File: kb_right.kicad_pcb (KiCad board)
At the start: 2 copper layers, 208.8 x 117.5 mm, 175 parts, among them J1 10029449-001RLF, J2 Conn_01x03, J3 Conn_01x06, J4 Conn_01x08, J5 Conn_01x09, SW0 RotaryEncoder_Switch

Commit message: added 1.75u right shift
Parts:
- added D32_1: D_Small, Diode_SMD:D_SOD-123, B.Cu at (197.9, 110.9)
- added MX32_1: MX-NoLED, MX_Only:MXOnly-1.75U-Hotswap, F.Cu at (162.7, 114.3)
- added MX32_2: MX-NoLED, MX_Only:MXOnly-1U-Hotswap, F.Cu at (188.9, 114.3)
- C101, C102, C103, C104, C105, C106, C107, C108, C109, C110, C111, C112, C113, C114, C115, C116, C117, C118, C119, C120, C121, C122, C123, C124, C125, C126, C127, C128, C129, C130, C131, C132, C133, C134, C135, C136, C137, C138, C139, C140, C141, C142: value C_Small -> 0.1uF
- MX32: footprint MX_Only:MXOnly-2.75U-Hotswap -> MX_Only:MXOnly-2.75U-Hotswap-ReversedStabilizers
- moved D32 27.5 mm to (155.6, 119.9)
- moved D133 17.9 mm to (172.2, 108.7), turned to 90 degrees
- moved C125 7.86 mm to (171.3, 102.5)
- moved D141 7.17 mm to (212.7, 143.7)
- moved D40 7.17 mm to (200.8, 143.7)
- moved D42 7.17 mm to (238.9, 143.7)
- moved D140 7.17 mm to (193.7, 143.7)
- moved D142 7.17 mm to (231.8, 143.7)
- moved D41 7.17 mm to (219.9, 143.7)
- moved D114 7.17 mm to (141.3, 81.8)
- moved D117 7.17 mm to (212.7, 81.8)
- moved D13 7.17 mm to (129.4, 81.8)
- moved D15 7.17 mm to (167.5, 81.8)
- moved D16 7.17 mm to (191.3, 81.8)
- moved D26 7.17 mm to (238.9, 81.8)
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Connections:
- J5 pad 1: /COL6 -> GND
- J5 pad 2: /ROW5 -> /COL6
- J5 pad 3: /ROW6 -> /ROW5
- J5 pad 4: /ROW7 -> /ROW6
- J5 pad 5: /ROW8 -> /ROW7
- J5 pad 6: /ROW9 -> /ROW8
- J5 pad 7: /COL7 -> /ROW9
- J5 pad 8: /COL8 -> /COL7
- J5 pad 9: GND -> /COL8
- MX32 pad 1: /COL6 -> /COL5
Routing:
- net /COL5: track 168.8 -> 210.3 mm, vias 5 -> 7
- net Net-(MX32-Pad2): track 9.53 -> 22.8 mm
- net +5V: track 1059.3 -> 1072.0 mm
- net /COL6: track 175.6 -> 166.0 mm
- net Net-(D133-Pad2): track 38.0 -> 47.1 mm
- net /ROW7: track 280.9 -> 289.9 mm
- net /ROW6: track 252.7 -> 261.1 mm
- net /COL8: track 188.4 -> 196.4 mm
- net /ROW5: track 251.4 -> 259.4 mm
- net Net-(D132-Pad2): track 31.2 -> 38.5 mm
- net /ROW8: track 290.1 -> 295.5 mm
- net Net-(D32_1-Pad2): track 0.00 -> 3.11 mm
- net /COL7: track 149.7 -> 151.2 mm
- net Net-(D134-Pad2): track 183.9 -> 182.7 mm
- net Net-(D127-Pad2): track 195.8 -> 196.5 mm
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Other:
- outline, holes or cut-outs redrawn

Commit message: revise right shfit route
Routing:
- net /COL5: track 210.3 -> 205.7 mm
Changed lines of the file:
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@@
   (segment (start 191.0655 42.14375) (end 189.536 42.14375) (width 0.254) (layer "B.Cu") (net 2))
   (segment (start 189.536 42.14375) (end 189.51575 42.164) (width 0.254) (layer "B.Cu") (net 2))
-  (segment (start 188.341 118.872) (end 192.405 114.808) (width 0.254) (layer "F.Cu") (net 3))
+  (segment (start 192.5828 114.6302) (end 192.5828 112.0902) (width 0.254) (layer "F.Cu") (net 3))
+  (segment (start 188.341 118.872) (end 192.5828 114.6302) (width 0.254) (layer "F.Cu") (net 3))
   (segment (start 194.08775 63.40475) (end 194.08775 36.576001) (width 0.254) (layer "F.Cu") (net 3))
   (segment (start 194.08775 36.576001) (end 194.052794 36.541045) (width 0.254) (layer "F.Cu") (net 3))
-  (segment (start 192.405 112.268) (end 194.1195 110.5535) (width 0.254) (layer "F.Cu") (net 3))
+  (segment (start 192.5828 112.0902) (end 194.1195 110.5535) (width 0.254) (layer "F.Cu") (net 3))
+  (segment (start 194.1195 110.5535) (end 194.1195 63.4365) (width 0.254) (layer "F.Cu") (net 3))
   (segment (start 194.1195 63.4365) (end 194.08775 63.40475) (width 0.254) (layer "F.Cu") (net 3))
-  (segment (start 192.405 114.808) (end 192.405 112.268) (width 0.254) (layer "F.Cu") (net 3))
-  (segment (start 194.1195 110.5535) (end 194.1195 63.4365) (width 0.254) (layer "F.Cu") (net 3))
   (via (at 194.08775 63.40475) (size 0.8) (drill 0.4) (layers "F.Cu" "B.Cu") (net 3))
   (via (at 194.052794 36.541045) (size 0.8) (drill 0.4) (layers "F.Cu" "B.Cu") (net 3))
@@
   (segment (start 51.8795 71.12) (end 53.18125 72.42175) (width 0.254) (layer "B.Cu") (net 12))
   (segment (start 53.18125 72.42175) (end 53.18125 80.10625) (width 0.254) (layer "B.Cu") (net 12))
+  (segment (start 195.326 114.935) (end 195.326 84.23627) (width 0.254) (layer "F.Cu") (net 13))
+  (segment (start 190.881 118.872) (end 191.389 118.872) (width 0.254) (layer "F.Cu") (net 13))
+  (segment (start 195.10375 84.01402) (end 195.10375 36.570286) (width 0.254) (layer "F.Cu") (net 13))
+  (segment (start 195.326 84.23627) (end 195.10375 84.01402) (width 0.254) (layer "F.Cu") (net 13))
+  (segment (start 195.10375 36.570286) (end 195.106606 36.56743) (width 0.254) (layer "F.Cu") (net 13))
   (segment (start 191.389 118.872) (end 195.326 114.935) (width 0.254) (layer "F.Cu") (net 13))
-  (segment (start 190.881 118.872) (end 191.389 118.872) (width 0.254) (layer "F.Cu") (net 13))
-  (segment (start 195.326 106.96575) (end 195.10375 106.7435) (width 0.254) (layer "F.Cu") (net 13))
-  (segment (start 195.10375 106.7435) (end 195.10375 84.01402) (width 0.254) (layer "F.Cu") (net 13))
-  (segment (start 195.10375 84.01402) (end 195.10375 36.570286) (width 0.254) (layer "F.Cu") (net 13))
-  (segment (start 195.326 114.935) (end 195.326 106.96575) (width 0.254) (layer "F.Cu") (net 13))
-  (segment (start 195.10375 36.570286) (end 195.106606 36.56743) (width 0.254) (layer "F.Cu") (net 13))
   (via (at 195.10375 84.01402) (size 0.8) (drill 0.4) (layers "F.Cu" "B.Cu") (net 13))
   (via (at 195.106606 36.56743) (size 0.8) (drill 0.4) (layers "F.Cu" "B.Cu") (net 13))
@@
   (segment (start 171.1115 106.426) (end 171.49375 106.04375) (width 0.254) (layer "B.Cu") (net 81))
   (segment (start 161.611979 105.414479) (end 162.6235 106.426) (width 0.254) (layer "B.Cu") (net 81))
+  (segment (start 177.68695 111.44375) (end 181.811329 115.568129) (width 0.254) (layer "B.Cu") (net 82))
+  (segment (start 183.2235 125.04848) (end 209.70473 125.04848) (width 0.254) (layer "B.Cu") (net 82))
+  (segment (start 172.99375 111.44375) (end 177.68695 111.44375) (width 0.254) (layer "B.Cu") (net 82))
+  (segment (start 181.811329 123.636309) (end 183.2235 125.04848) (width 0.254) (layer "B.Cu") (net 82))
+  (segment (start 181.811329 115.568129) (end 181.811329 123.636309) (width 0.254) (layer "B.Cu") (net 82))
   (segment (start 209.70473 125.04848) (end 210.025 125.36875) (width 0.254) (layer "B.Cu") (net 82))
-  (segment (start 183.2235 125.04848) (end 209.70473 125.04848) (width 0.254) (layer "B.Cu") (net 82))
-  (segment (start 181.811329 123.636309) (end 183.2235 125.04848) (width 0.254) (layer "B.Cu") (net 82))
-  (segment (start 181.811329 116.279329) (end 181.811329 123.636309) (width 0.254) (layer "B.Cu") (net 82))
-  (segment (start 172.99375 111.44375) (end 176.97575 111.44375) (width 0.254) (layer "B.Cu") (net 82))
-  (segment (start 176.97575 111.44375) (end 181.811329 116.279329) (width 0.254) (layer "B.Cu") (net 82))
   (segment (start 169.675022 126.20625) (end 67.037447 126.20625) (width 0.254) (layer "B.Cu") (net 83))
   (segment (start 222.25 126.65075) (end 219.86875 129.032) (width 0.254) (layer "B.Cu") (net 83))
@@
   (segment (start 129.44 110.61225) (end 128.55575 109.728) (width 0.254) (layer "B.Cu") (net 98))
   (segment (start 187.289786 42.766018) (end 187.289786 40.883694) (width 0.254) (layer "B.Cu") (net 98))
-  (segment (start 152.146 117.221) (end 150.01875 115.09375) (width 0.254) (layer "F.Cu") (net 99))
+  (segment (start 176.655269 111.8616) (end 161.8996 111.8616) (width 0.254) (layer "F.Cu") (net 99))
+  (segment (start 159.921479 109.883479) (end 155.419521 109.883479) (width 0.254) (layer "F.Cu") (net 99))
   (segment (start 145.115979 75.615229) (end 145.115979 90.963696) (width 0.254) (layer "F.Cu") (net 99))
   (segment (start 142.65275 73.152) (end 145.115979 75.615229) (width 0.254) (layer "F.Cu") (net 99))
   (segment (start 165.27246 60.50179) (end 186.157586 60.50179) (width 0.254) (layer "F.Cu") (net 99))
-  (segment (start 174.117 120.904) (end 170.434 117.221) (width 0.254) (layer "F.Cu") (net 99))
   (segment (start 144.498 61.78925) (end 148.1455 65.43675) (width 0.254) (layer "F.Cu") (net 99))
   (segment (start 150.01875 110.58525) (end 150.01875 124.841) (width 0.254) (layer "F.Cu") (net 99))
-  (segment (start 178.562 120.904) (end 174.117 120.904) (width 0.254) (layer "F.Cu") (net 99))
   (segment (start 188.016286 44.470992) (end 188.016286 43.488085) (width 0.254) (layer "F.Cu") (net 99))
   (segment (start 161.0995 64.67475) (end 165.27246 60.50179) (width 0.254) (layer "F.Cu") (net 99))
   (segment (start 188.289266 58.37011) (end 188.289266 44.743972) (width 0.254) (layer "F.Cu") (net 99))
-  (segment (start 178.689 120.777) (end 178.562 120.904) (width 0.254) (layer "F.Cu") (net 99))
   (segment (start 150.01875 124.841) (end 153.95575 128.778) (width 0.254) (layer "F.Cu") (net 99))
   (segment (start 186.157586 60.50179) (end 188.289266 58.37011) (width 0.254) (layer "F.Cu") (net 99))
@@
   (segment (start 188.289266 44.743972) (end 188.016286 44.470992) (width 0.254) (layer "F.Cu") (net 99))
   (segment (start 160.3375 65.43675) (end 161.0995 64.67475) (width 0.254) (layer "F.Cu") (net 99))
+  (segment (start 179.324 114.530331) (end 176.655269 111.8616) (width 0.254) (layer "F.Cu") (net 99))
+  (segment (start 155.419521 109.883479) (end 153.543 111.76) (width 0.254) (layer "F.Cu") (net 99))
   (segment (start 143.7005 61.78925) (end 144.498 61.78925) (width 0.254) (layer "F.Cu") (net 99))
+  (segment (start 161.8996 111.8616) (end 159.921479 109.883479) (width 0.254) (layer "F.Cu") (net 99))
   (segment (start 141.950979 72.450229) (end 142.65275 73.152) (width 0.254) (layer "F.Cu") (net 99))
   (segment (start 143.7005 61.78925) (end 141.950979 63.538771) (width 0.254) (layer "F.Cu") (net 99))
   (segment (start 141.950979 63.538771) (end 141.950979 72.450229) (width 0.254) (layer "F.Cu") (net 99))
   (segment (start 153.543 111.76) (end 151.1935 111.76) (width 0.254) (layer "F.Cu") (net 99))
-  (segment (start 170.434 117.221) (end 152.146 117.221) (width 0.254) (layer "F.Cu") (net 99))
+  (segment (start 179.324 114.7064) (end 179.324 114.530331) (width 0.254) (layer "F.Cu") (net 99))
   (via (at 145.115979 90.963696) (size 0.8) (drill 0.4) (layers "F.Cu" "B.Cu") (net 99))
   (via (at 153.95575 128.778) (size 0.8) (drill 0.4) (layers "F.Cu" "B.Cu") (net 99))
-  (via (at 178.689 120.777) (size 0.8) (drill 0.4) (layers "F.Cu" "B.Cu") (net 99))
   (via (at 188.016286 43.488085) (size 0.8) (drill 0.4) (layers "F.Cu" "B.Cu") (net 99))
+  (via (at 179.324 114.7064) (size 0.8) (drill 0.4) (layers "F.Cu" "B.Cu") (net 99))
   (via (at 143.7005 61.78925) (size 0.8) (drill 0.4) (layers "F.Cu" "B.Cu") (net 99))
   (via (at 153.543 111.76) (size 0.8) (drill 0.4) (layers "F.Cu" "B.Cu") (net 99))
   (via (at 141.950979 72.450229) (size 0.8) (drill 0.4) (layers "F.Cu" "B.Cu") (net 99))
   (segment (start 141.284229 71.783479) (end 141.950979 72.450229) (width 0.254) (layer "B.Cu") (net 99))
+  (segment (start 179.32875 116.84) (end 179.32875 114.71115) (width 0.254) (layer "B.Cu") (net 99))
   (segment (start 155.63375 130.81) (end 155.63375 130.456) (width 0.254) (layer "B.Cu") (net 99))
   (segment (start 140.841521 90.833479) (end 144.985762 90.833479) (width 0.254) (layer "B.Cu") (net 99))
   (segment (start 136.079021 71.783479) (end 141.284229 71.783479) (width 0.254) (layer "B.Cu") (net 99))
   (segment (start 189.671104 39.14375) (end 191.0655 39.14375) (width 0.254) (layer "B.Cu") (net 99))
-  (segment (start 178.689 120.777) (end 179.32875 120.13725) (width 0.254) (layer "B.Cu") (net 99))
   (segment (start 143.7005 61.78925) (end 143.7275 61.76225) (width 0.254) (layer "B.Cu") (net 99))
   (segment (start 155.63375 111.76) (end 153.543 111.76) (width 0.254) (layer "B.Cu") (net 99))
   (segment (start 144.985762 90.833479) (end 145.115979 90.963696) (width 0.254) (layer "B.Cu") (net 99))
   (segment (start 188.016286 40.798568) (end 189.671104 39.14375) (width 0.254) (layer "B.Cu") (net 99))
-  (segment (start 179.32875 120.13725) (end 179.32875 116.84) (width 0.254) (layer "B.Cu") (net 99))
+  (segment (start 179.32875 114.71115) (end 179.324 114.7064) (width 0.254) (layer "B.Cu") (net 99))
   (segment (start 143.7275 61.76225) (end 143.7275 54.61) (width 0.254) (layer "B.Cu") (net 99))
   (segment (start 134.2025 73.66) (end 136.079021 71.783479) (width 0.254) (layer "B.Cu") (net 99))

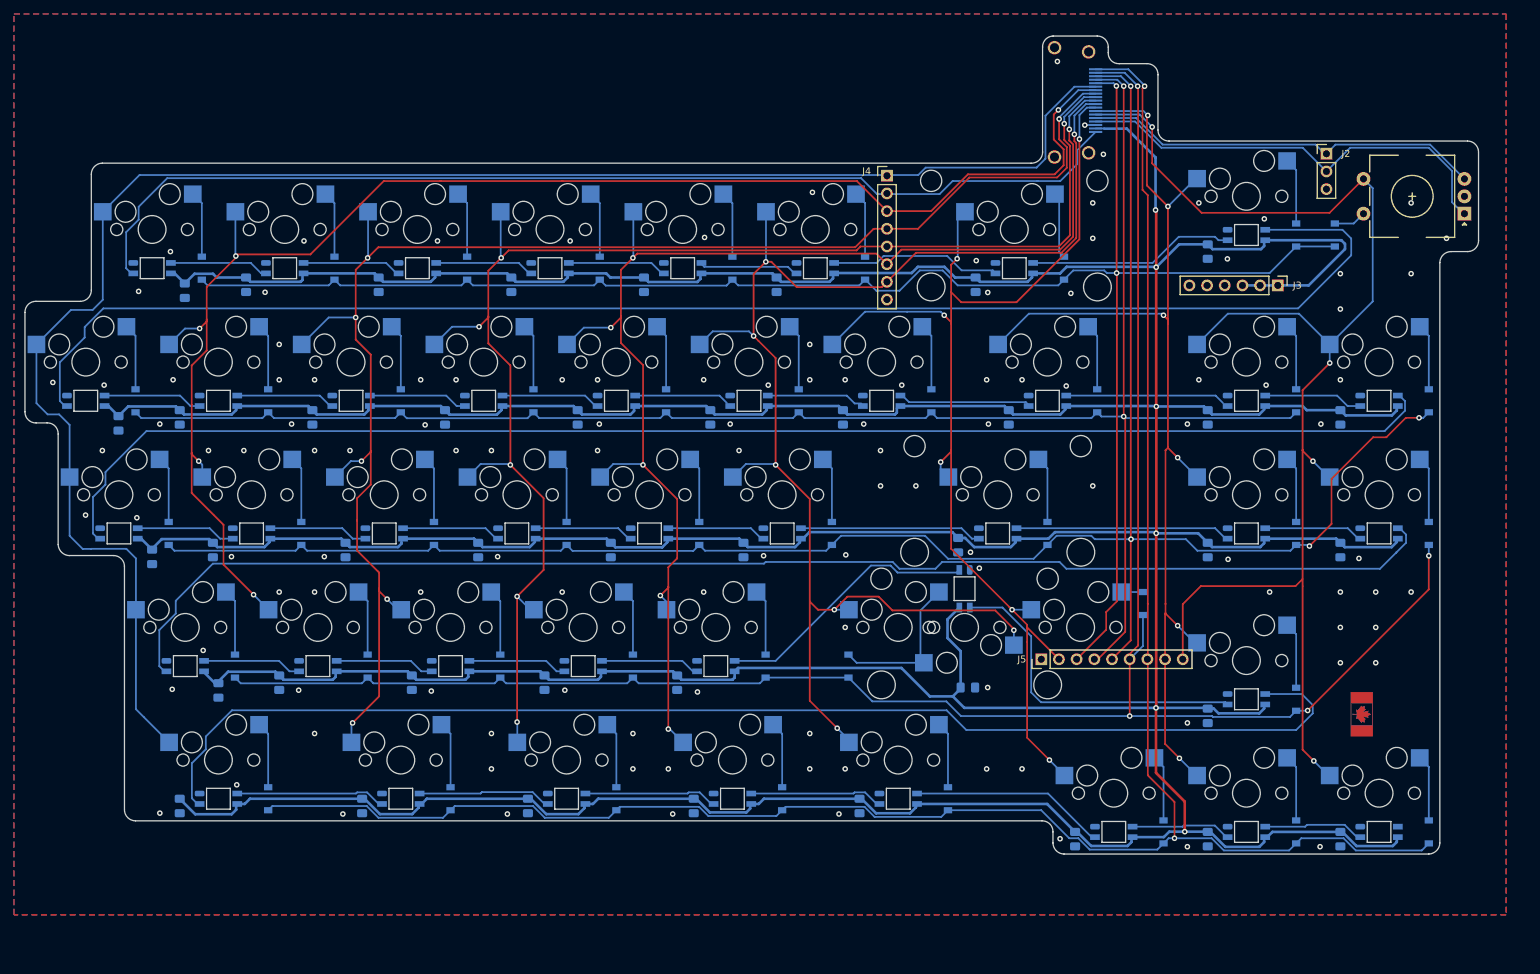
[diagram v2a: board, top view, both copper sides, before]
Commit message: fixed split right shift
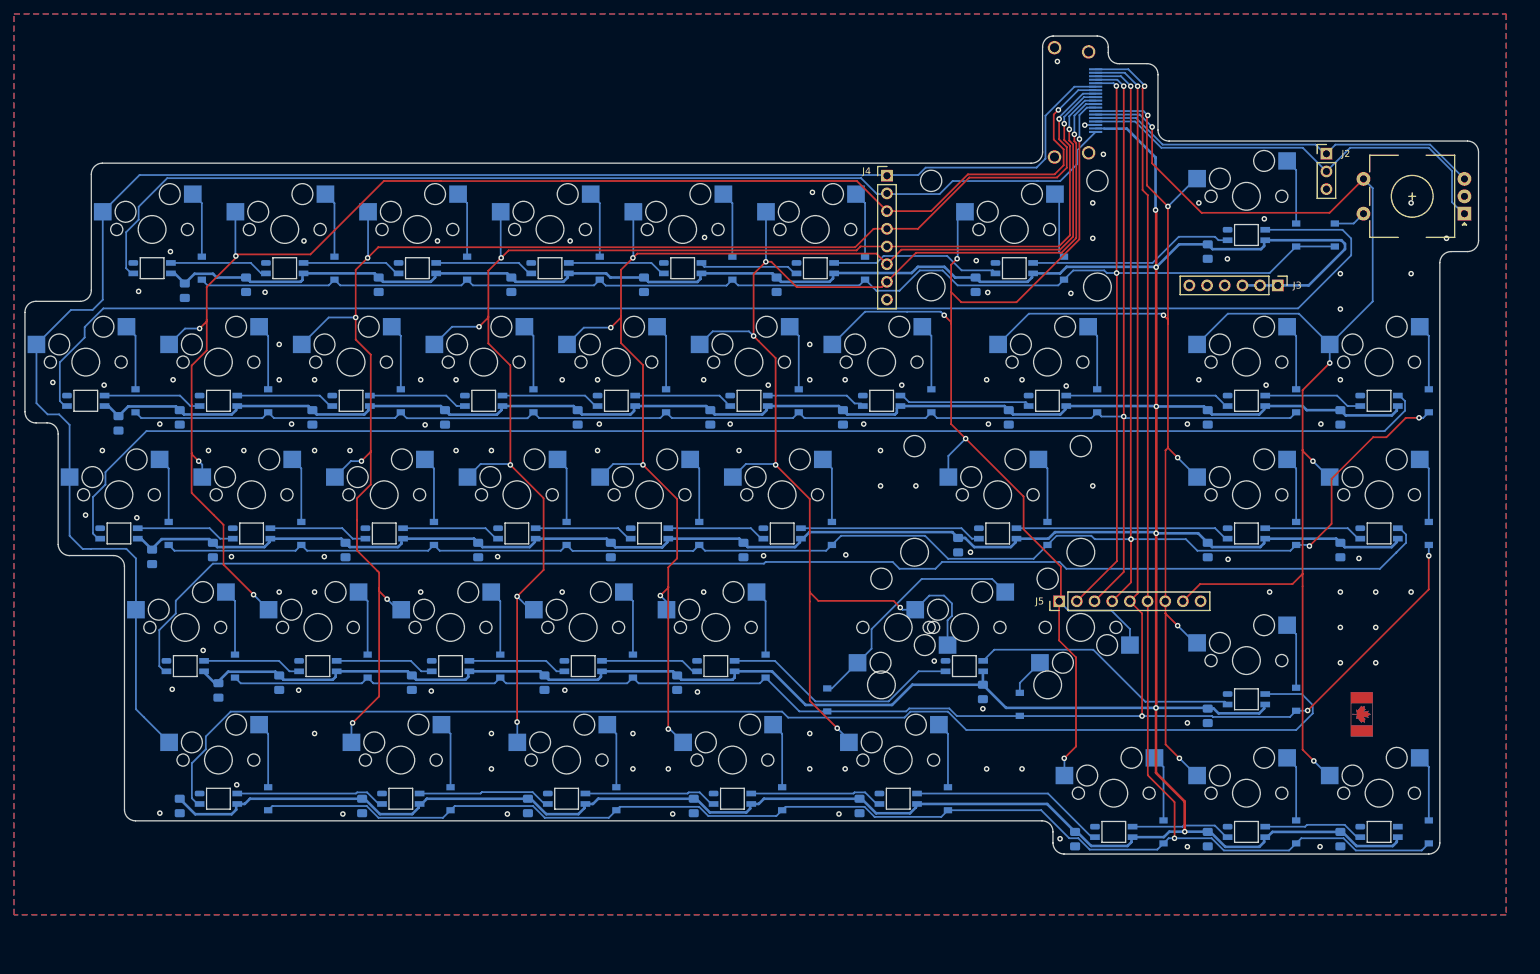
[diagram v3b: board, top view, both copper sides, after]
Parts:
- MX32: footprint MX_Only:MXOnly-2.75U-Hotswap-ReversedStabilizers -> MX_Only:MXOnly-2.75U-Hotswap
- moved D32_1 22.9 mm to (180.2, 125.3)
- moved D133 11.1 mm to (172.2, 119.9), turned to 180 degrees
- moved J5 8.72 mm to (185.8, 110.5)
- moved D32 5.73 mm to (152.5, 124.7)
- moved C133 2.25 mm to (174.9, 123.6), turned to -90 degrees
- turned MX32 to 0 degrees
- turned MX32_1 to 180 degrees
- turned MX32_2 to 180 degrees
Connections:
- J5 pad 1: GND -> /COL6
- J5 pad 2: /COL6 -> /ROW5
- J5 pad 3: /ROW5 -> /ROW6
- J5 pad 4: /ROW6 -> /ROW7
- J5 pad 5: /ROW7 -> /ROW8
- J5 pad 6: /ROW8 -> /ROW9
- J5 pad 7: /ROW9 -> /COL7
- J5 pad 8: /COL7 -> /COL8
- J5 pad 9: /COL8 -> GND
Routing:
- net Net-(D32-Pad2): track 22.8 -> 34.5 mm
- net +5V: track 1072.0 -> 1061.2 mm
- net /ROW6: track 261.1 -> 252.3 mm
- net Net-(D133-Pad2): track 47.5 -> 39.0 mm
- net /ROW7: track 289.9 -> 281.5 mm
- net /ROW5: track 259.4 -> 251.1 mm
- net /COL6: track 166.0 -> 174.0 mm, vias 6 -> 5
- net /COL5: track 205.7 -> 197.8 mm, vias 7 -> 6
- net /COL8: track 196.4 -> 188.6 mm
- net /ROW8: track 295.5 -> 289.4 mm
- net Net-(D132-Pad2): track 38.5 -> 34.5 mm
- net Net-(D32_1-Pad2): track 3.11 -> 5.52 mm
- net Net-(D134-Pad2): track 182.7 -> 183.3 mm
- net GND: vias 121 -> 120
